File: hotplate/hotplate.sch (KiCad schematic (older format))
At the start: 26 parts, among them J1 1x10_Male, J2 1x6_Male, J3 1x7_Male, SW1 PWR, SW2 MOT, SW3 HT, U1 LM317T

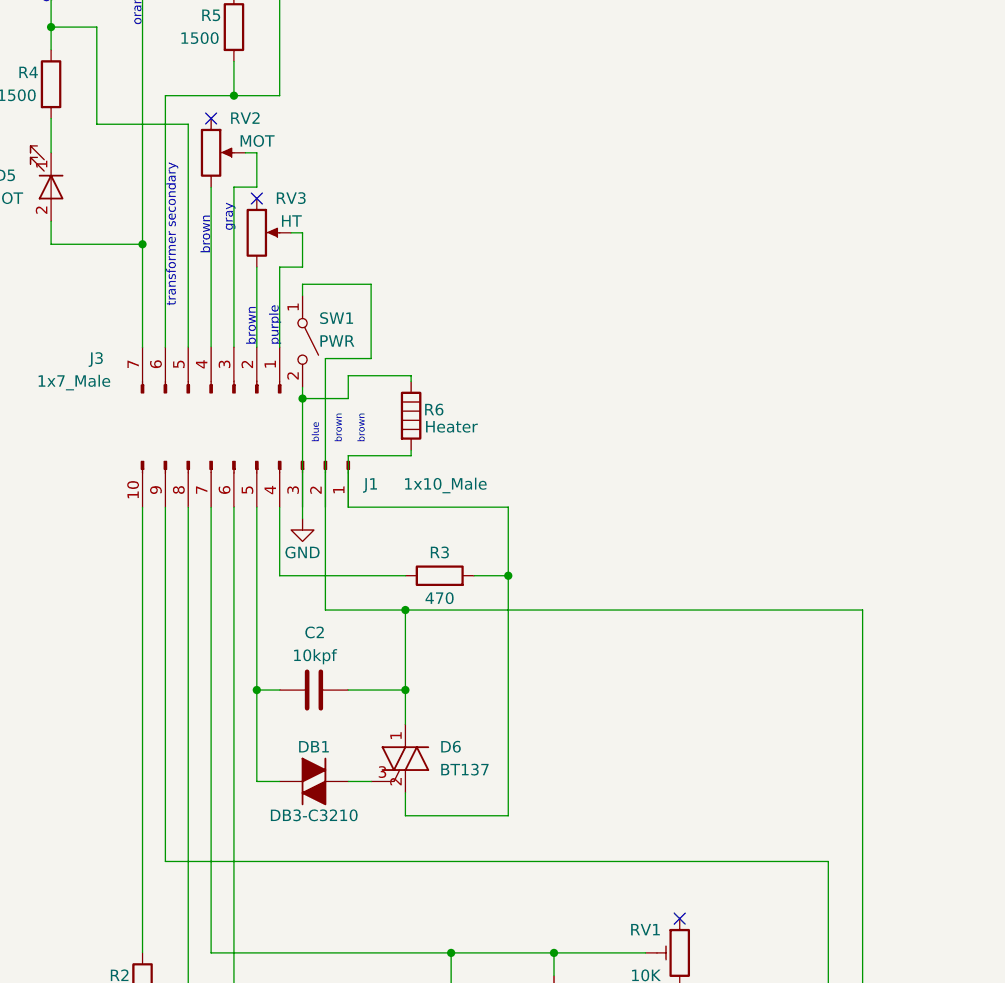
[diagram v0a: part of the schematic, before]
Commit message: Update with additions to hotplate and datasheets.
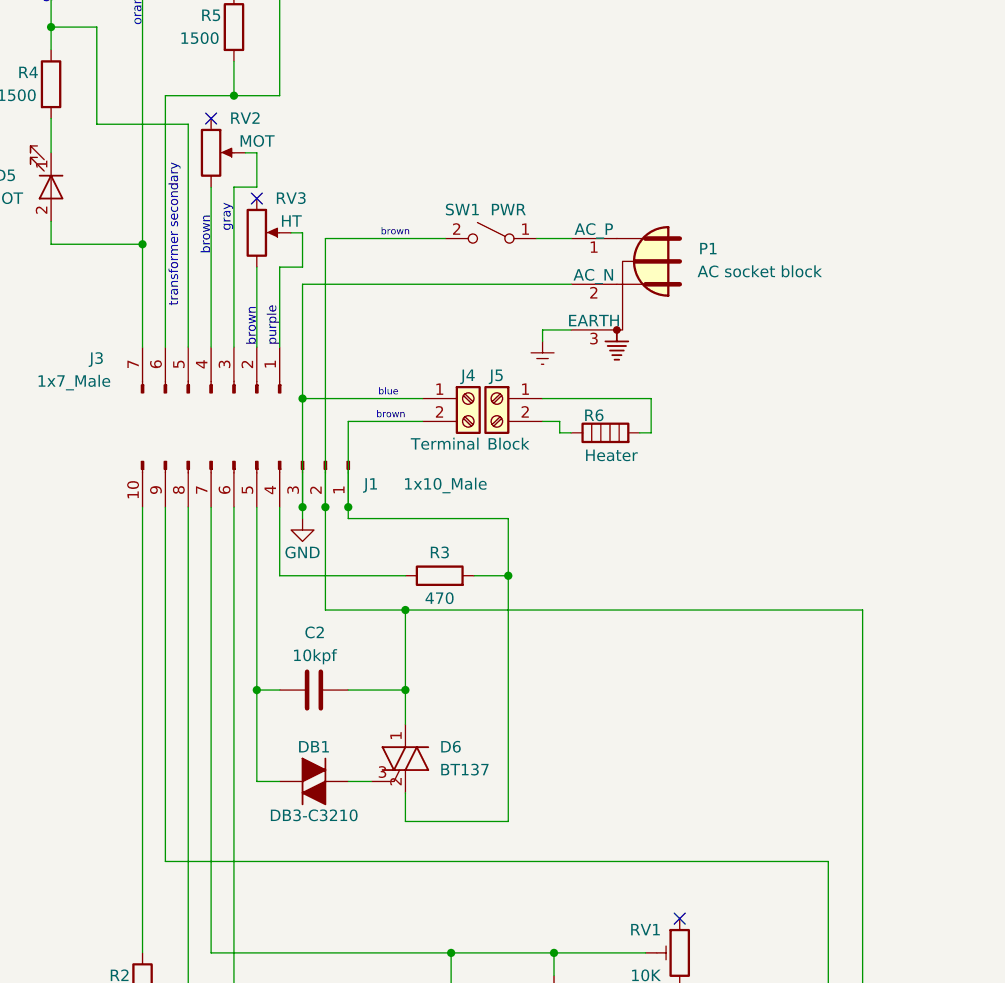
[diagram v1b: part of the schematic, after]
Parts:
- added J4: Terminal, symbol Screw_Terminal_01x02
- added J5: Block, symbol Screw_Terminal_01x02
- added P1: AC socket block, symbol Conn_WallPlug_Earth
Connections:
- net GND: now also J1.3 (Pin_3), J4.1 (Pin_1), P1.2 (AC_N); no longer R6.1, SW1.2 (B)
- net at C2.2, D6.1 (A1), J2.6 (Pin_6): now also J1.2 (Pin_2), SW1.2 (B); no longer SW1.1 (A)
- net at D6.2 (A2), J1.1 (Pin_1), R3.2: now also J4.2 (Pin_2); no longer R6.2
- new net: P1.1 (AC_P), SW1.1 (A)
- new net: J5.2 (Pin_2), R6.1
- new net: J5.1 (Pin_1), R6.2
- new net Earth: P1.3 (EARTH)
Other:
- moved on the sheet: R6, SW1
